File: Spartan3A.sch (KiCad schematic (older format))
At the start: 32 parts, among them P1 JTAG_FPGA, Q1 Q_NMOS_DSG, U1 XC3S50A/VQ100, U6 M25P20, U7 XO53

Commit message: All Resistors 0805, New Buttons
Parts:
- R1, R2, R3: footprint Resistors_SMD:R_0603_HandSoldering -> Resistors_SMD:R_0805_HandSoldering
- R16: value 180R -> 100R; footprint Resistors_SMD:R_0603_HandSoldering -> Resistors_SMD:R_0805_HandSoldering
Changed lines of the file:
@@
 F 0 "R3" V 12430 6550 50  0000 C CNN
 F 1 "4k7" V 12350 6550 50  0000 C CNN
-F 2 "Resistors_SMD:R_0603_HandSoldering" V 12280 6550 50  0001 C CNN
+F 2 "Resistors_SMD:R_0805_HandSoldering" V 12280 6550 50  0001 C CNN
 F 3 "" H 12350 6550 50  0000 C CNN
 	1    12350 6550
@@
 F 0 "R2" V 3430 2900 50  0000 C CNN
 F 1 "330R" V 3350 2900 50  0000 C CNN
-F 2 "Resistors_SMD:R_0603_HandSoldering" V 3280 2900 50  0001 C CNN
+F 2 "Resistors_SMD:R_0805_HandSoldering" V 3280 2900 50  0001 C CNN
 F 3 "" H 3350 2900 50  0000 C CNN
 	1    3350 2900
@@
 F 0 "R1" V 3230 2900 50  0000 C CNN
 F 1 "4k7" V 3150 2900 50  0000 C CNN
-F 2 "Resistors_SMD:R_0603_HandSoldering" V 3080 2900 50  0001 C CNN
+F 2 "Resistors_SMD:R_0805_HandSoldering" V 3080 2900 50  0001 C CNN
 F 3 "" H 3150 2900 50  0000 C CNN
 	1    3150 2900
@@
 P 2850 8500
 F 0 "R16" V 2930 8500 50  0000 C CNN
-F 1 "180R" V 2850 8500 50  0000 C CNN
-F 2 "Resistors_SMD:R_0603_HandSoldering" V 2780 8500 50  0001 C CNN
+F 1 "100R" V 2850 8500 50  0000 C CNN
+F 2 "Resistors_SMD:R_0805_HandSoldering" V 2780 8500 50  0001 C CNN
 F 3 "" H 2850 8500 50  0000 C CNN
 	1    2850 8500

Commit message: Ready for Production
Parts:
- removed GS1, GS2, GS3: VS, Connect:GS2, symbol GS2
- removed Q1: Q_NMOS_DSG, TO_SOT_Packages_SMD:SOT-23_Handsoldering, symbol Q_NMOS_DSG
- removed R2: 330R, Resistors_SMD:R_0805_HandSoldering, symbol R
- removed S1: MO, Buttons_Switches_ThroughHole:SW_DIP_x3_Slide, symbol SW_DIP_x3
- added Q1: BSS123, TO_SOT_Packages_SMD:SOT-23_Handsoldering, symbol Q_NMOS_GSD
- added SW3: SW_Push, SMD_Switch_LSX1301:SW_LSx_1301, symbol SW_Push
- added SW4: SW_DIP_x02, w_switch:dip_2-300, symbol SW_DIP_x02
- D1: value LED_DONE -> Green; symbol LED -> LED-RESCUE-FPGABoard
- R16: value 100R -> 36R
- U7: value XO53 -> 50MHz
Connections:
- net labels added: M1, M2
- wire segments 199 -> 189
- no-connect marks 6 -> 10
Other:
- moved on the sheet: R16, R3

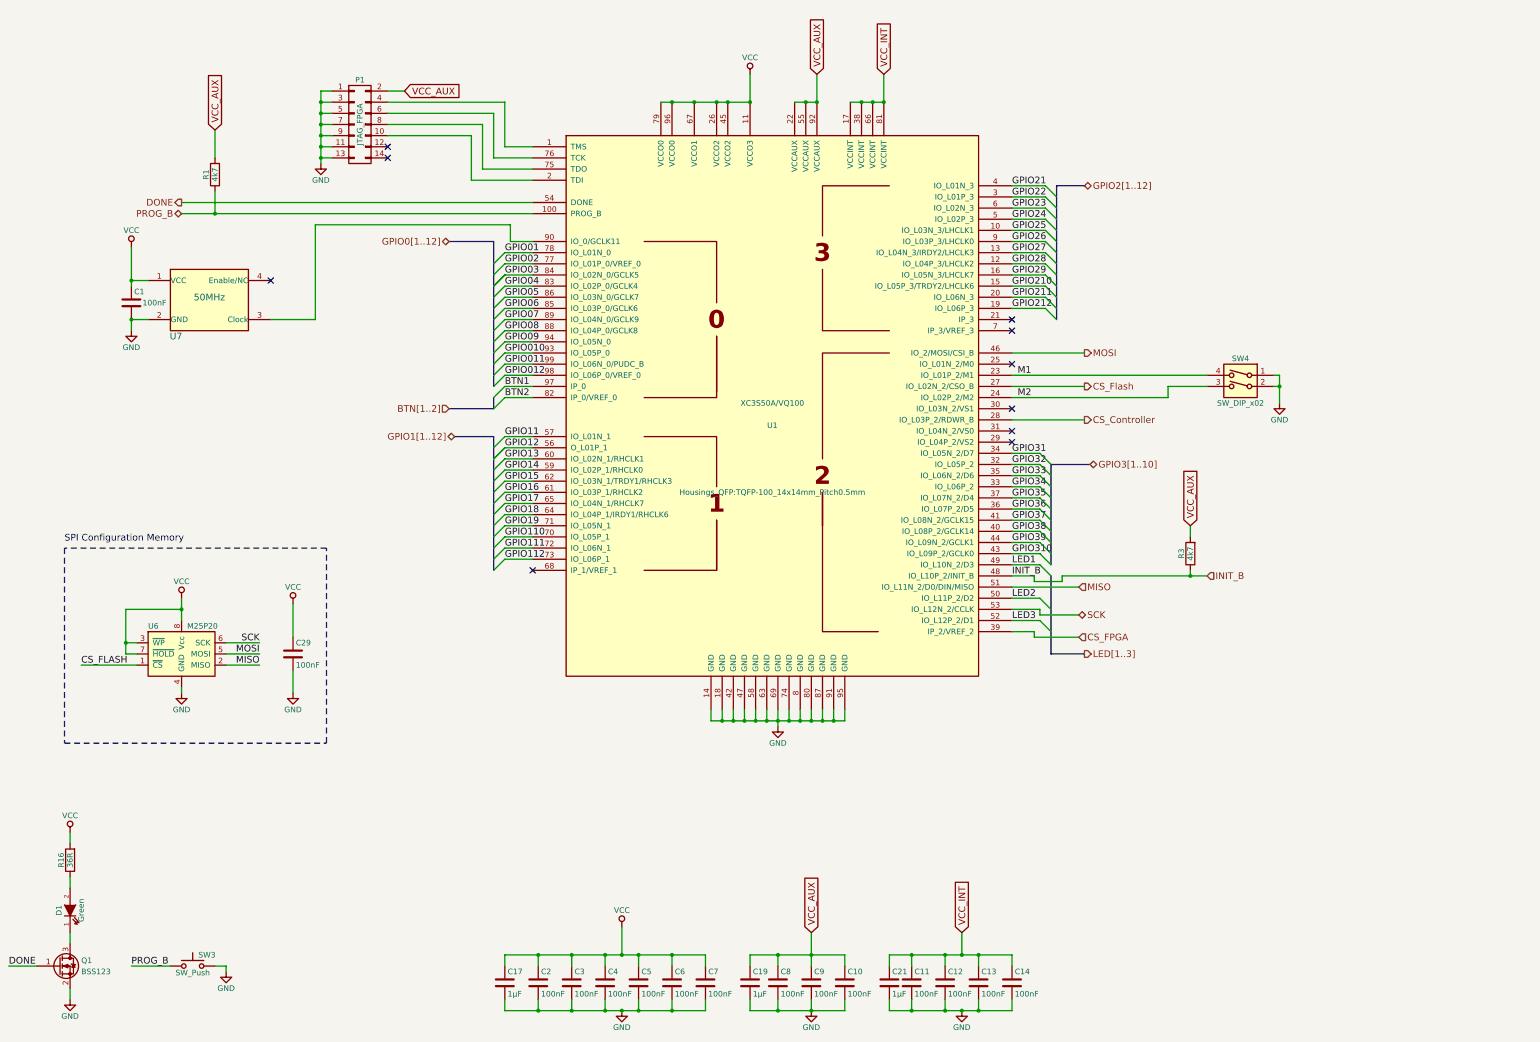
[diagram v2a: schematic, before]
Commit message: Changed SPI Connection to support Multi-Master
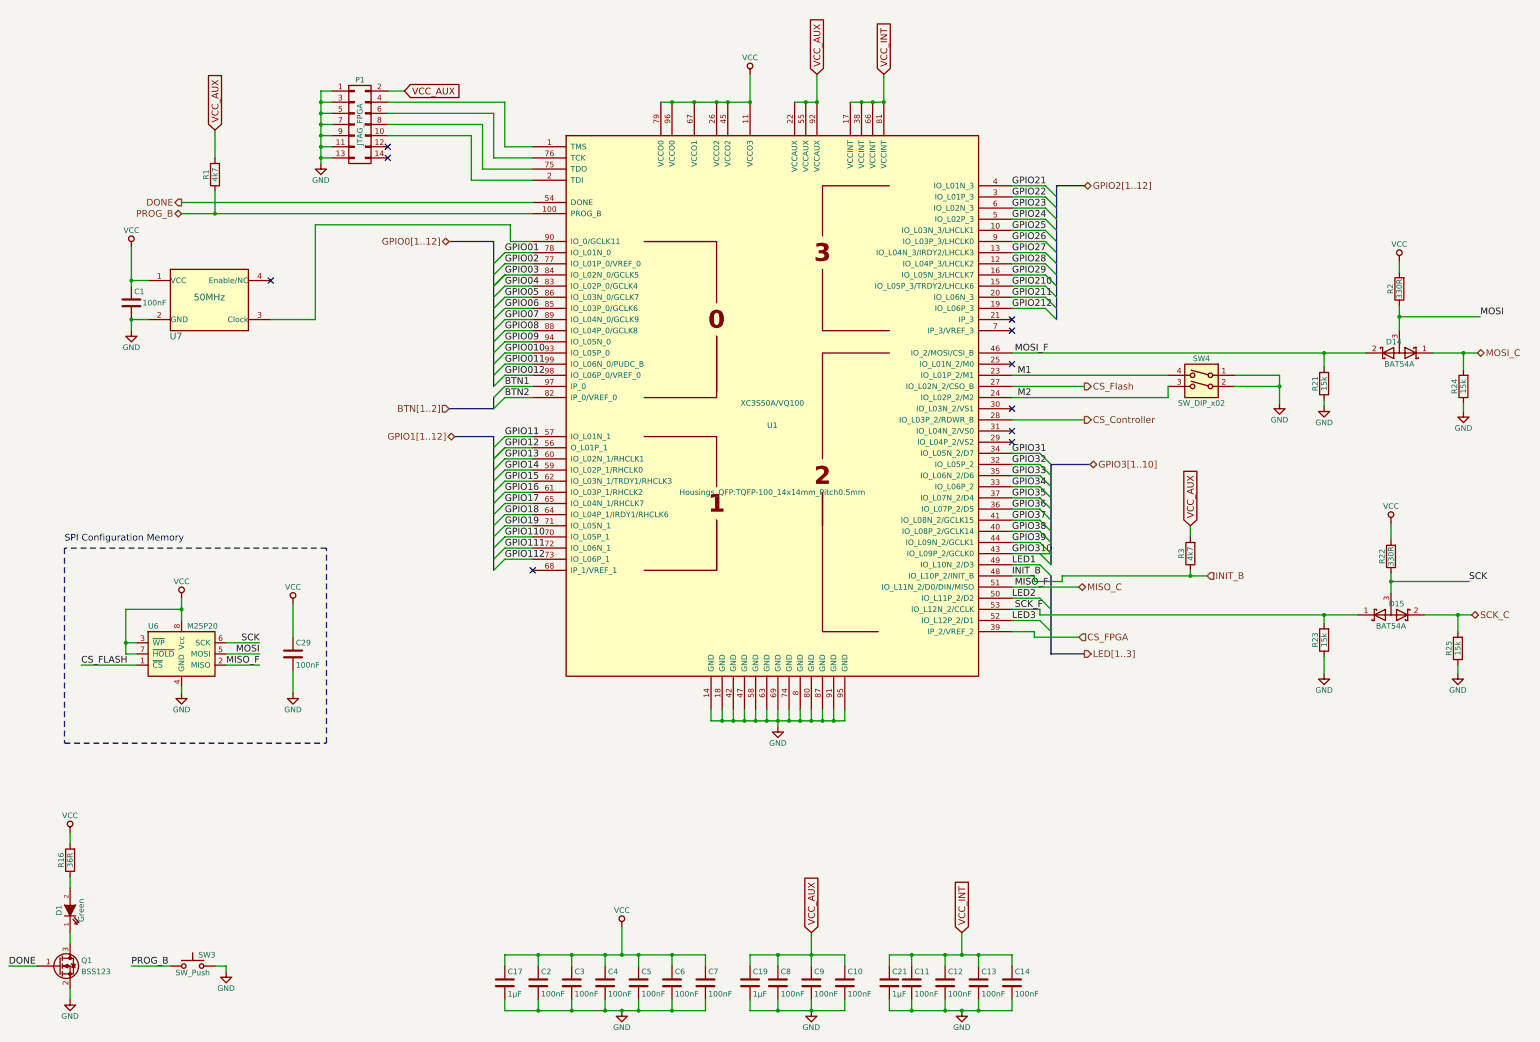
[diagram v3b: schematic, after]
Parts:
- added D14, D15: BAT54A, TO_SOT_Packages_SMD:SOT-23, symbol D_Schottky_x2_ACom_KKA
- added R2, R22: 330R, Resistors_SMD:R_0805_HandSoldering, symbol R
- added R21, R23, R24, R25: 15k, Resistors_SMD:R_0805_HandSoldering, symbol R
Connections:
- net GND: now also R21.1, R23.1, R24.1, R25.1
- net MOSI: now also D14.3 (A), R2.1; no longer U1.46 (IO_2/MOSI/CSI_B)
- net SCK: now also D15.3 (A), R22.1; no longer U1.53 (IO_L12N_2/CCLK)
- net VCC: now also R2.2, R22.2
- net MISO renamed MISO_C
- new net MOSI_C: D14.1 (K), R24.2
- new net MOSI_F: D14.2 (K), R21.2, U1.46 (IO_2/MOSI/CSI_B)
- new net SCK_C: D15.2 (K), R25.2
- new net SCK_F: D15.1 (K), R23.2, U1.53 (IO_L12N_2/CCLK)
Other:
- moved on the sheet: SW4

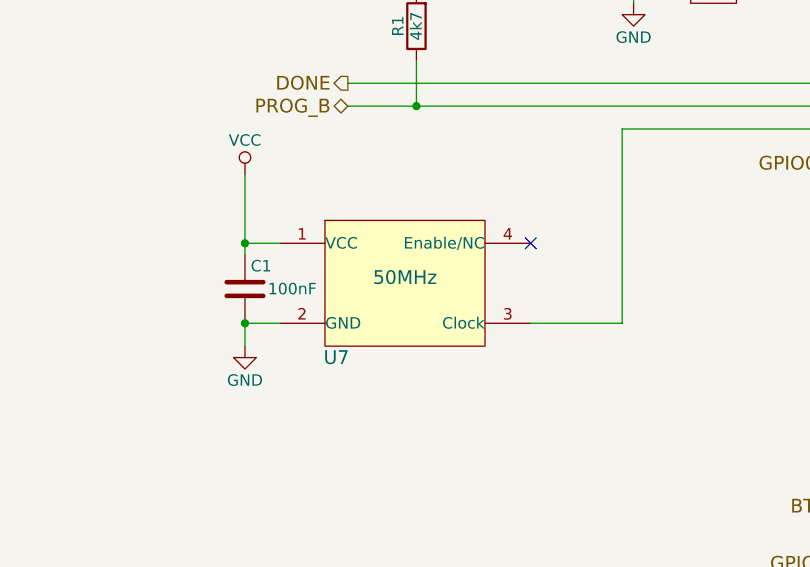
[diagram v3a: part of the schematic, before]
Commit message: Added Resistor in Reset Line
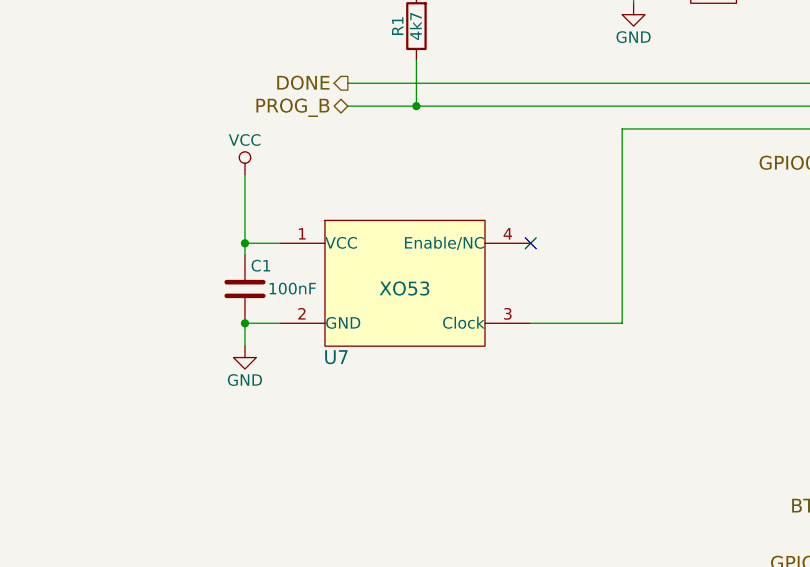
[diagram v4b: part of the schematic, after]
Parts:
- U7: value 50MHz -> XO53
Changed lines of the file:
@@
 $EndComp
 $Comp
-L GND #PWR01
+L GND #PWR2
 U 1 1 5748F443
 P 4100 2800
-F 0 "#PWR01" H 4100 2550 50  0001 C CNN
+F 0 "#PWR2" H 4100 2550 50  0001 C CNN
 F 1 "GND" H 4100 2650 50  0000 C CNN
 F 2 "" H 4100 2800 50  0000 C CNN
@@
 NoConn ~ 4700 2750
 $Comp
-L GND #PWR02
+L GND #PWR16
 U 1 1 5748F44F
 P 8200 7850
-F 0 "#PWR02" H 8200 7600 50  0001 C CNN
+F 0 "#PWR16" H 8200 7600 50  0001 C CNN
 F 1 "GND" H 8200 7700 50  0000 C CNN
 F 2 "" H 8200 7850 50  0000 C CNN
@@
 $EndComp
 $Comp
-L GND #PWR03
+L GND #PWR23
 U 1 1 5748F4A8
 P 9850 10400
-F 0 "#PWR03" H 9850 10150 50  0001 C CNN
+F 0 "#PWR23" H 9850 10150 50  0001 C CNN
 F 1 "GND" H 9850 10250 50  0000 C CNN
 F 2 "" H 9850 10400 50  0000 C CNN
@@
 $EndComp
 $Comp
-L GND #PWR04
+L GND #PWR22
 U 1 1 5748F4C4
 P 8500 10400
-F 0 "#PWR04" H 8500 10150 50  0001 C CNN
+F 0 "#PWR22" H 8500 10150 50  0001 C CNN
 F 1 "GND" H 8500 10250 50  0000 C CNN
 F 2 "" H 8500 10400 50  0000 C CNN
@@
 $EndComp
 $Comp
-L GND #PWR05
+L GND #PWR21
 U 1 1 5748F4E6
 P 6800 10400
-F 0 "#PWR05" H 6800 10150 50  0001 C CNN
+F 0 "#PWR21" H 6800 10150 50  0001 C CNN
 F 1 "GND" H 6800 10250 50  0000 C CNN
 F 2 "" H 6800 10400 50  0000 C CNN
@@
 	10600 4100 10700 4200
 $Comp
-L GND #PWR06
+L GND #PWR6
 U 1 1 57828260
 P 12700 4950
-F 0 "#PWR06" H 12700 4700 50  0001 C CNN
+F 0 "#PWR6" H 12700 4700 50  0001 C CNN
 F 1 "GND" H 12700 4800 50  0000 C CNN
 F 2 "" H 12700 4950 50  0000 C CNN
@@
 $EndComp
 $Comp
-L GND #PWR07
+L GND #PWR14
 U 1 1 57830E2E
 P 2850 7550
-F 0 "#PWR07" H 2850 7300 50  0001 C CNN
+F 0 "#PWR14" H 2850 7300 50  0001 C CNN
 F 1 "GND" H 2850 7400 50  0000 C CNN
 F 2 "" H 2850 7550 50  0000 C CNN
@@
 $EndComp
 $Comp
-L GND #PWR08
+L GND #PWR15
 U 1 1 578324A6
 P 3850 7550
-F 0 "#PWR08" H 3850 7300 50  0001 C CNN
+F 0 "#PWR15" H 3850 7300 50  0001 C CNN
 F 1 "GND" H 3850 7400 50  0000 C CNN
 F 2 "" H 3850 7550 50  0000 C CNN
@@
 CS_FPGA
 $Comp
-L GND #PWR09
+L GND #PWR5
 U 1 1 5748F50A
 P 2400 4300
-F 0 "#PWR09" H 2400 4050 50  0001 C CNN
+F 0 "#PWR5" H 2400 4050 50  0001 C CNN
 F 1 "GND" H 2400 4150 50  0000 C CNN
 F 2 "" H 2400 4300 50  0000 C CNN
@@
 $EndComp
 $Comp
-L GND #PWR010
+L GND #PWR20
 U 1 1 5783F7F7
 P 1850 10300
-F 0 "#PWR010" H 1850 10050 50  0001 C CNN
+F 0 "#PWR20" H 1850 10050 50  0001 C CNN
 F 1 "GND" H 1850 10150 50  0000 C CNN
 F 2 "" H 1850 10300 50  0000 C CNN
@@
 DONE
 $Comp
-L VCC #PWR011
+L VCC #PWR1
 U 1 1 5786CFE3
 P 7950 2000
-F 0 "#PWR011" H 7950 1850 50  0001 C CNN
+F 0 "#PWR1" H 7950 1850 50  0001 C CNN
 F 1 "VCC" H 7950 2150 50  0000 C CNN
 F 2 "" H 7950 2000 50  0000 C CNN
@@
 VCC_AUX
 $Comp
-L VCC #PWR012
+L VCC #PWR11
 U 1 1 5786E3E9
 P 3850 6750
-F 0 "#PWR012" H 3850 6600 50  0001 C CNN
+F 0 "#PWR11" H 3850 6600 50  0001 C CNN
 F 1 "VCC" H 3850 6900 50  0000 C CNN
 F 2 "" H 3850 6750 50  0000 C CNN
@@
 $EndComp
 $Comp
-L VCC #PWR013
+L VCC #PWR10
 U 1 1 5786E437
 P 2850 6700
-F 0 "#PWR013" H 2850 6550 50  0001 C CNN
+F 0 "#PWR10" H 2850 6550 50  0001 C CNN
 F 1 "VCC" H 2850 6850 50  0000 C CNN
 F 2 "" H 2850 6700 50  0000 C CNN
@@
 $EndComp
 $Comp
-L VCC #PWR014
+L VCC #PWR17
 U 1 1 5786E6C9
 P 1850 8800
-F 0 "#PWR014" H 1850 8650 50  0001 C CNN
+F 0 "#PWR17" H 1850 8650 50  0001 C CNN
 F 1 "VCC" H 1850 8950 50  0000 C CNN
 F 2 "" H 1850 8800 50  0000 C CNN
@@
 $EndComp
 $Comp
-L VCC #PWR015
+L VCC #PWR18
 U 1 1 5786EDEE
 P 6800 9650
-F 0 "#PWR015" H 6800 9500 50  0001 C CNN
+F 0 "#PWR18" H 6800 9500 50  0001 C CNN
 F 1 "VCC" H 6800 9800 50  0000 C CNN
 F 2 "" H 6800 9650 50  0000 C CNN
@@
 VCC_INT
 $Comp
-L VCC #PWR016
+L VCC #PWR3
 U 1 1 5787091E
 P 2400 3550
-F 0 "#PWR016" H 2400 3400 50  0001 C CNN
+F 0 "#PWR3" H 2400 3400 50  0001 C CNN
 F 1 "VCC" H 2400 3700 50  0000 C CNN
 F 2 "" H 2400 3550 50  0000 C CNN
@@
 $EndComp
 $Comp
-L XO53 U7
-U 1 1 57936089
-P 3000 4050
-F 0 "U7" H 2800 3750 60  0000 C CNN
-F 1 "50MHz" H 3100 4100 60  0000 C CNN
-F 2 "Oscillator__Crystal_SMD:Oscillator_XO53" H 3100 4450 60  0001 C CNN
-F 3 "" H 2950 3900 60  0000 C CNN
-	1    3000 4050
-	1    0    0    -1
-$EndComp
-NoConn ~ 3650 3850
-$Comp
 L Q_NMOS_GSD Q1
 U 1 1 58A6573D
@@
 $EndComp
 $Comp
-L GND #PWR017
+L GND #PWR19
 U 1 1 58B11500
 P 3250 10050
-F 0 "#PWR017" H 3250 9800 50  0001 C CNN
+F 0 "#PWR19" H 3250 9800 50  0001 C CNN
 F 1 "GND" H 3250 9900 50  0000 C CNN
 F 2 "" H 3250 10050 50  0000 C CNN
@@
 $EndComp
 $Comp
-L VCC #PWR018
+L VCC #PWR4
 U 1 1 58BA93EC
 P 13775 3675
-F 0 "#PWR018" H 13775 3525 50  0001 C CNN
+F 0 "#PWR4" H 13775 3525 50  0001 C CNN
 F 1 "VCC" H 13775 3825 50  0000 C CNN
 F 2 "" H 13775 3675 50  0000 C CNN
@@
 $EndComp
 $Comp
-L VCC #PWR019
+L VCC #PWR9
 U 1 1 58BA9730
 P 13700 6025
-F 0 "#PWR019" H 13700 5875 50  0001 C CNN
+F 0 "#PWR9" H 13700 5875 50  0001 C CNN
 F 1 "VCC" H 13700 6175 50  0000 C CNN
 F 2 "" H 13700 6025 50  0000 C CNN
@@
 $EndComp
 $Comp
-L GND #PWR020
+L GND #PWR12
 U 1 1 58BABD21
 P 13100 7375
-F 0 "#PWR020" H 13100 7125 50  0001 C CNN
+F 0 "#PWR12" H 13100 7125 50  0001 C CNN
 F 1 "GND" H 13100 7225 50  0000 C CNN
 F 2 "" H 13100 7375 50  0000 C CNN
@@
 $EndComp
 $Comp
-L GND #PWR021
+L GND #PWR7
 U 1 1 58BAC5DE
 P 13100 4975
-F 0 "#PWR021" H 13100 4725 50  0001 C CNN
+F 0 "#PWR7" H 13100 4725 50  0001 C CNN
 F 1 "GND" H 13100 4825 50  0000 C CNN
 F 2 "" H 13100 4975 50  0000 C CNN
@@
 $EndComp
 $Comp
-L GND #PWR022
+L GND #PWR8
 U 1 1 58BAC907
 P 14350 5025
-F 0 "#PWR022" H 14350 4775 50  0001 C CNN
+F 0 "#PWR8" H 14350 4775 50  0001 C CNN
 F 1 "GND" H 14350 4875 50  0000 C CNN
 F 2 "" H 14350 5025 50  0000 C CNN
@@
 Connection ~ 14300 6850
 $Comp
-L GND #PWR023
+L GND #PWR13
 U 1 1 58BADEB6
 P 14300 7375
-F 0 "#PWR023" H 14300 7125 50  0001 C CNN
+F 0 "#PWR13" H 14300 7125 50  0001 C CNN
 F 1 "GND" H 14300 7225 50  0000 C CNN
 F 2 "" H 14300 7375 50  0000 C CNN
@@
 Wire Wire Line
 	4050 4200 3650 4200
+NoConn ~ 3650 3850
+$Comp
+L XO53 U7
+U 1 1 58BE3C06
+P 3000 4050
+F 0 "U7" H 2800 3750 60  0000 C CNN
+F 1 "XO53" H 3100 4050 60  0000 C CNN
+F 2 "Oscillator__Crystal_SMD:Oscillator_XO53" H 3100 4450 60  0001 C CNN
+F 3 "" H 2950 3900 60  0000 C CNN
+	1    3000 4050
+	1    0    0    -1
+$EndComp
 $EndSCHEMATC
